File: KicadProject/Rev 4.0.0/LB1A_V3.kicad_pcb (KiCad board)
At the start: 6 copper layers, 42 x 42 mm, 187 parts, among them J601 2337019-1, J602 2337019-1, U101 STM32MP157CAA3, U201 AS4C256M16D3LC-12BCN, U401 STPMIC1xPQR, U501 S40FC004C1B2C00000, U601 LBEE59B1LV-278, U701 DF40C-70DP-0.4V(51), U702 DF40C-100DP-0.4V(51), U703 DF40C-100DP-0.4V(51), X101 32.768kHz, Y101 24MHz

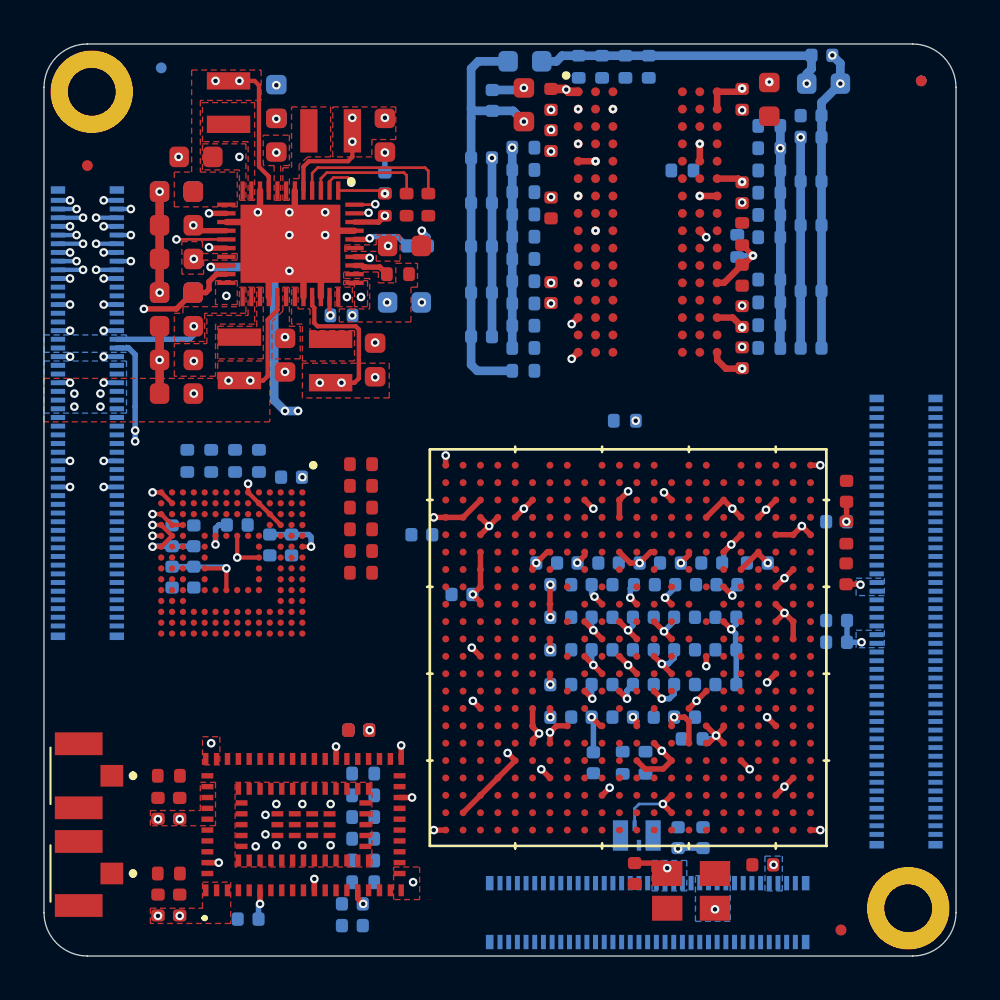
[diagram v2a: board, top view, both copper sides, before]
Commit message: ram power routing
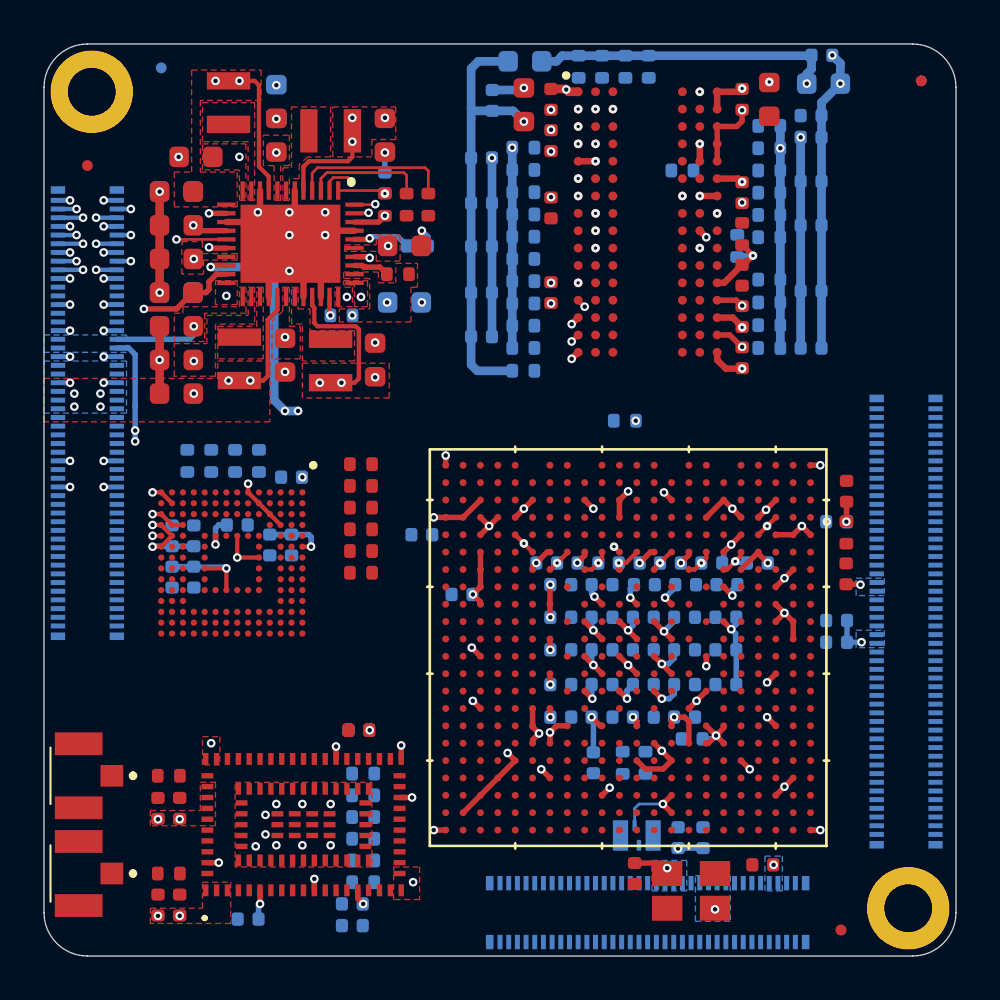
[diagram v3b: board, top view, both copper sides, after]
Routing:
- net PMIC_VOUT2_VDD_DDR: track 9.31 -> 26.5 mm, vias 11 -> 32
- net GND: track 203.8 -> 203.0 mm, vias 161 -> 162
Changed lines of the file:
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@@
     (thickness 1.2)
     (drawings 8)
-    (tracks 751)
+    (tracks 814)
     (zones 0)
     (modules 187)
@@
   (layers
     (0 L1_Sig_Pwr.Cu mixed)
-    (1 L2_Gnd.Cu power hide)
+    (1 L2_Gnd.Cu power)
     (2 L3_Sig_Pwr.Cu mixed)
-    (3 L4_Sig_Gnd.Cu mixed hide)
-    (4 L5_Gnd_Pwr.Cu power hide)
+    (3 L4_Sig_Gnd.Cu mixed)
+    (4 L5_Gnd_Pwr.Cu power)
     (31 L6_Sig_Pwr.Cu mixed)
     (32 B.Adhes user hide)
@@
   )
   (setup
-    (last_trace_width 0.254)
+    (last_trace_width 0.2)
     (user_trace_width 0.1)
     (user_trace_width 0.127)
@@
   (gr_arc (start 173 128) (end 171 128) (angle -90) (layer Edge.Cuts) (width 0.05))
   (gr_arc (start 173 90) (end 173 88) (angle -90) (layer Edge.Cuts) (width 0.05))
+  (via (at 207.05 110) (size 0.4) (drill 0.15) (layers L1_Sig_Pwr.Cu L6_Sig_Pwr.Cu) (net 9))
+  (via (at 201.2 97.4) (size 0.4) (drill 0.15) (layers L1_Sig_Pwr.Cu L6_Sig_Pwr.Cu) (net 9))
+  (via (at 202 95.8) (size 0.4) (drill 0.15) (layers L1_Sig_Pwr.Cu L6_Sig_Pwr.Cu) (net 9))
+  (via (at 200.4 95) (size 0.4) (drill 0.15) (layers L1_Sig_Pwr.Cu L6_Sig_Pwr.Cu) (net 9))
+  (via (at 201.2 90.2) (size 0.4) (drill 0.15) (layers L1_Sig_Pwr.Cu L6_Sig_Pwr.Cu) (net 9))
+  (via (at 196.4 97.4) (size 0.4) (drill 0.15) (layers L1_Sig_Pwr.Cu L6_Sig_Pwr.Cu) (net 9))
+  (via (at 196.4 95.8) (size 0.4) (drill 0.15) (layers L1_Sig_Pwr.Cu L6_Sig_Pwr.Cu) (net 9))
+  (via (at 195.6 94.2) (size 0.4) (drill 0.15) (layers L1_Sig_Pwr.Cu L6_Sig_Pwr.Cu) (net 9))
+  (via (at 196.4 92.6) (size 0.4) (drill 0.15) (layers L1_Sig_Pwr.Cu L6_Sig_Pwr.Cu) (net 9))
+  (via (at 195.6 91.8) (size 0.4) (drill 0.15) (layers L1_Sig_Pwr.Cu L6_Sig_Pwr.Cu) (net 9))
+  (via (at 196.4 91) (size 0.4) (drill 0.15) (layers L1_Sig_Pwr.Cu L6_Sig_Pwr.Cu) (net 9))
   (via (at 203.15 91.05) (size 0.4) (drill 0.2) (layers L1_Sig_Pwr.Cu L6_Sig_Pwr.Cu) (net 9))
   (via (at 203.15 95.3) (size 0.4) (drill 0.2) (layers L1_Sig_Pwr.Cu L6_Sig_Pwr.Cu) (net 9))
@@
   (segment (start 198.93 111.4) (end 198.43 111.9) (width 0.254) (layer L1_Sig_Pwr.Cu) (net 1))
   (segment (start 199.1 111.4) (end 198.93 111.4) (width 0.254) (layer L1_Sig_Pwr.Cu) (net 1))
-  (segment (start 198 111.9) (end 198.43 111.9) (width 0.254) (layer L1_Sig_Pwr.Cu) (net 1))
-  (segment (start 197.5 111.4) (end 198 111.9) (width 0.254) (layer L1_Sig_Pwr.Cu) (net 1))
   (segment (start 196.22 116.52) (end 196.3 116.6) (width 0.254) (layer L6_Sig_Pwr.Cu) (net 1))
   (segment (start 196.22 115.9) (end 196.22 116.52) (width 0.254) (layer L6_Sig_Pwr.Cu) (net 1))
@@
   (segment (start 188.68 96.88) (end 188.4 96.6) (width 0.254) (layer L6_Sig_Pwr.Cu) (net 1))
   (segment (start 188.68 97.3) (end 188.68 96.88) (width 0.254) (layer L6_Sig_Pwr.Cu) (net 1))
+  (via (at 197.25 111.15) (size 0.4) (drill 0.15) (layers L1_Sig_Pwr.Cu L6_Sig_Pwr.Cu) (net 1))
+  (segment (start 197.5 111.4) (end 197.25 111.15) (width 0.2) (layer L1_Sig_Pwr.Cu) (net 1))
   (via (at 186.7 94.89) (size 0.4) (drill 0.15) (layers L1_Sig_Pwr.Cu L6_Sig_Pwr.Cu) (net 2))
   (segment (start 186.56 94.75) (end 186.7 94.89) (width 0.127) (layer L1_Sig_Pwr.Cu) (net 2))
@@
   (segment (start 195.15 90.2) (end 195.05 90.1) (width 0.4) (layer L1_Sig_Pwr.Cu) (net 9))
   (segment (start 195.6 90.2) (end 195.15 90.2) (width 0.4) (layer L1_Sig_Pwr.Cu) (net 9))
+  (via (at 195.3 101.7) (size 0.4) (drill 0.2) (layers L1_Sig_Pwr.Cu L6_Sig_Pwr.Cu) (net 9))
+  (segment (start 195.6 101.4) (end 195.3 101.7) (width 0.2) (layer L1_Sig_Pwr.Cu) (net 9))
+  (via (at 195.9 100.1) (size 0.4) (drill 0.2) (layers L1_Sig_Pwr.Cu L6_Sig_Pwr.Cu) (net 9))
+  (segment (start 195.6 99.8) (end 195.9 100.1) (width 0.2) (layer L1_Sig_Pwr.Cu) (net 9))
+  (segment (start 202 93.4) (end 202 92.6) (width 0.254) (layer L1_Sig_Pwr.Cu) (net 9))
+  (segment (start 202 92.6) (end 202 91.8) (width 0.254) (layer L1_Sig_Pwr.Cu) (net 9))
+  (segment (start 202 91.8) (end 202.9 91.8) (width 0.254) (layer L1_Sig_Pwr.Cu) (net 9))
+  (segment (start 203.15 91.55) (end 203.15 91.05) (width 0.254) (layer L1_Sig_Pwr.Cu) (net 9))
+  (segment (start 202.9 91.8) (end 203.15 91.55) (width 0.254) (layer L1_Sig_Pwr.Cu) (net 9))
+  (segment (start 202.88 99.8) (end 203.15 100.07) (width 0.254) (layer L1_Sig_Pwr.Cu) (net 9))
+  (segment (start 202 99.8) (end 202.88 99.8) (width 0.254) (layer L1_Sig_Pwr.Cu) (net 9))
+  (segment (start 202.58 101.4) (end 203.15 101.97) (width 0.254) (layer L1_Sig_Pwr.Cu) (net 9))
+  (segment (start 202 101.4) (end 202.58 101.4) (width 0.254) (layer L1_Sig_Pwr.Cu) (net 9))
+  (via (at 193.1 111) (size 0.4) (drill 0.15) (layers L1_Sig_Pwr.Cu L6_Sig_Pwr.Cu) (net 9))
+  (segment (start 192.700001 110.600001) (end 193.1 111) (width 0.2) (layer L1_Sig_Pwr.Cu) (net 9))
+  (segment (start 193.5 111.4) (end 193.1 111) (width 0.2) (layer L1_Sig_Pwr.Cu) (net 9))
+  (segment (start 193.500001 111.4) (end 193.5 111.4) (width 0.2) (layer L1_Sig_Pwr.Cu) (net 9))
+  (via (at 194.63 111.9) (size 0.4) (drill 0.15) (layers L1_Sig_Pwr.Cu L6_Sig_Pwr.Cu) (net 9))
+  (segment (start 194.33 112.2) (end 194.63 111.9) (width 0.2) (layer L1_Sig_Pwr.Cu) (net 9))
+  (segment (start 194.3 112.2) (end 194.33 112.2) (width 0.2) (layer L1_Sig_Pwr.Cu) (net 9))
+  (segment (start 195.1 111.43) (end 194.63 111.9) (width 0.2) (layer L1_Sig_Pwr.Cu) (net 9))
+  (segment (start 195.1 111.4) (end 195.1 111.43) (width 0.2) (layer L1_Sig_Pwr.Cu) (net 9))
+  (segment (start 196.23 112.2) (end 196.53 111.9) (width 0.2) (layer L1_Sig_Pwr.Cu) (net 9))
+  (via (at 196.53 111.9) (size 0.4) (drill 0.15) (layers L1_Sig_Pwr.Cu L6_Sig_Pwr.Cu) (net 9))
+  (segment (start 195.9 112.2) (end 196.23 112.2) (width 0.2) (layer L1_Sig_Pwr.Cu) (net 9))
+  (segment (start 196.7 111.73) (end 196.53 111.9) (width 0.2) (layer L1_Sig_Pwr.Cu) (net 9))
+  (segment (start 196.7 111.4) (end 196.7 111.73) (width 0.2) (layer L1_Sig_Pwr.Cu) (net 9))
+  (segment (start 199.1 112.17) (end 199.37 111.9) (width 0.2) (layer L1_Sig_Pwr.Cu) (net 9))
+  (via (at 199.37 111.9) (size 0.4) (drill 0.15) (layers L1_Sig_Pwr.Cu L6_Sig_Pwr.Cu) (net 9))
+  (segment (start 199.1 112.2) (end 199.1 112.17) (width 0.2) (layer L1_Sig_Pwr.Cu) (net 9))
+  (segment (start 199.87 111.4) (end 199.37 111.9) (width 0.2) (layer L1_Sig_Pwr.Cu) (net 9))
+  (segment (start 199.9 111.4) (end 199.87 111.4) (width 0.2) (layer L1_Sig_Pwr.Cu) (net 9))
+  (via (at 201.27 111.9) (size 0.4) (drill 0.15) (layers L1_Sig_Pwr.Cu L6_Sig_Pwr.Cu) (net 9))
+  (segment (start 200.97 112.2) (end 201.27 111.9) (width 0.2) (layer L1_Sig_Pwr.Cu) (net 9))
+  (segment (start 200.7 112.2) (end 200.97 112.2) (width 0.2) (layer L1_Sig_Pwr.Cu) (net 9))
+  (segment (start 201.5 111.67) (end 201.27 111.9) (width 0.2) (layer L1_Sig_Pwr.Cu) (net 9))
+  (segment (start 201.5 111.4) (end 201.5 111.67) (width 0.2) (layer L1_Sig_Pwr.Cu) (net 9))
+  (via (at 202.832629 111.82568) (size 0.4) (drill 0.15) (layers L1_Sig_Pwr.Cu L6_Sig_Pwr.Cu) (net 9))
+  (segment (start 203.099999 111.55831) (end 202.832629 111.82568) (width 0.2) (layer L1_Sig_Pwr.Cu) (net 9))
+  (segment (start 203.099999 111.4) (end 203.099999 111.55831) (width 0.2) (layer L1_Sig_Pwr.Cu) (net 9))
+  (segment (start 202.458309 112.2) (end 202.832629 111.82568) (width 0.2) (layer L1_Sig_Pwr.Cu) (net 9))
+  (segment (start 202.3 112.2) (end 202.458309 112.2) (width 0.2) (layer L1_Sig_Pwr.Cu) (net 9))
+  (segment (start 202.906949 111.9) (end 202.832629 111.82568) (width 0.2) (layer L6_Sig_Pwr.Cu) (net 9))
+  (segment (start 203.37 111.9) (end 202.906949 111.9) (width 0.2) (layer L6_Sig_Pwr.Cu) (net 9))
+  (via (at 204.3 110.2) (size 0.4) (drill 0.15) (layers L1_Sig_Pwr.Cu L6_Sig_Pwr.Cu) (net 9))
+  (segment (start 203.899999 110.600001) (end 204.3 110.2) (width 0.2) (layer L1_Sig_Pwr.Cu) (net 9))
+  (segment (start 204.699999 109.800001) (end 204.3 110.2) (width 0.2) (layer L1_Sig_Pwr.Cu) (net 9))
+  (via (at 197.47 111.9) (size 0.4) (drill 0.15) (layers L1_Sig_Pwr.Cu L6_Sig_Pwr.Cu) (net 9))
+  (segment (start 197.8 111.9) (end 197.47 111.9) (width 0.2) (layer L1_Sig_Pwr.Cu) (net 9))
+  (segment (start 198.3 111.4) (end 197.8 111.9) (width 0.2) (layer L1_Sig_Pwr.Cu) (net 9))
+  (segment (start 197.5 111.93) (end 197.47 111.9) (width 0.2) (layer L1_Sig_Pwr.Cu) (net 9))
+  (segment (start 197.5 112.2) (end 197.5 111.93) (width 0.2) (layer L1_Sig_Pwr.Cu) (net 9))
   (segment (start 185.3 103.6) (end 184.7 103.6) (width 0.2) (layer L1_Sig_Pwr.Cu) (net 10))
   (segment (start 185.5 103.4) (end 185.3 103.6) (width 0.2) (layer L1_Sig_Pwr.Cu) (net 10))
@@
     (polygon
       (pts
-        (xy 213 112.6) (xy 193.1 112.6) (xy 193.1 110.9) (xy 186.6 110.9) (xy 186.593086 103.396543)
+        (xy 213 112.6) (xy 192.8 112.6) (xy 192.8 110.9) (xy 186.6 110.9) (xy 186.593086 103.396543)
         (xy 193.3 103.403457) (xy 193.3 90.6) (xy 178.5 90.6) (xy 178.5 88) (xy 213 88)
       )
@@
       (pts
         (xy 178.4 90.7) (xy 193.2 90.7) (xy 193.2 103.3) (xy 186.5 103.3) (xy 186.5 111)
-        (xy 193 111) (xy 193 112.7) (xy 213 112.7) (xy 213 130) (xy 171 130)
+        (xy 192.7 111) (xy 192.7 112.7) (xy 213 112.7) (xy 213 130) (xy 171 130)
         (xy 171 88) (xy 178.4 88)
       )
